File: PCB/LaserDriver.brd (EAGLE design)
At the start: 160 x 100 mm, 23 parts, among them IC1 OPA27U, IC2 7805T, Q1 IRF510

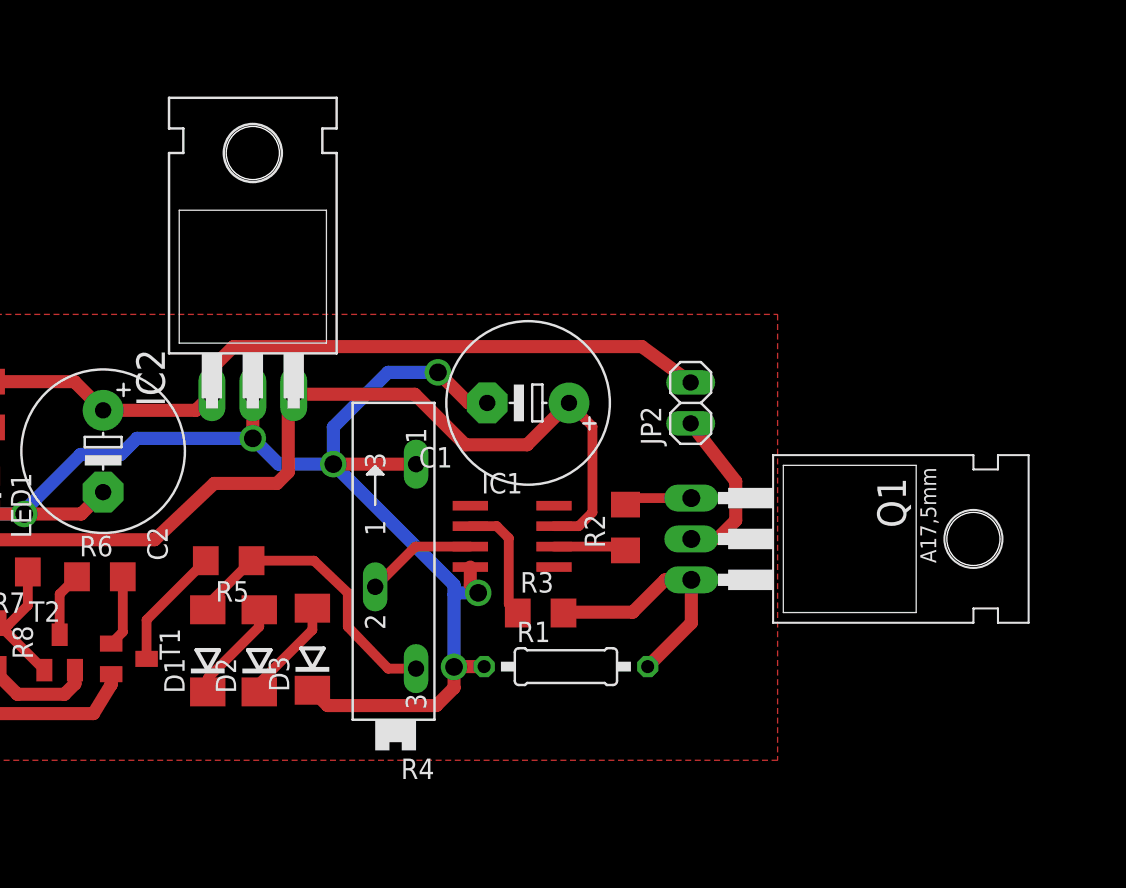
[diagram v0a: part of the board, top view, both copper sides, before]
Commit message: Fixed component placement issues and modified directory tree.
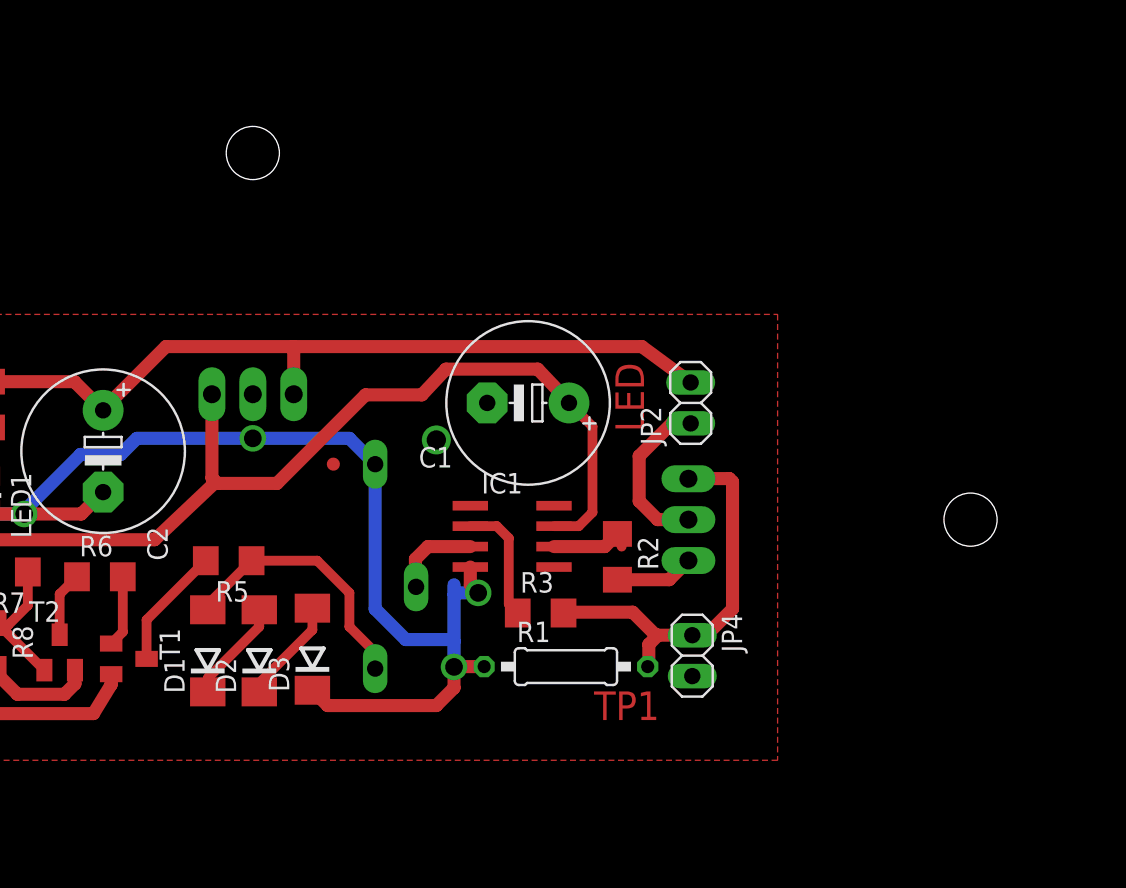
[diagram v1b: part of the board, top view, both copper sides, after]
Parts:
- added JP4: (no value), pinhead:1X02
- moved R2 1.89 mm to (58.4, 32.9), turned to 270 degrees
- moved Q1 1.21 mm to (69.1, 35.2), flipped to the bottom, turned to 90 degrees
- flipped IC2 to the bottom
- flipped R4 to the bottom
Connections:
- net GND: now also JP4.2
- net N$1: now also JP4.1
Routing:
- net GND: track 119.2 -> 104.0 mm, vias 8 -> 6
- net N$1: track 15.3 -> 24.8 mm
- net VCC: track 85.7 -> 87.9 mm
- net N$15: track 52.6 -> 54.7 mm
- net N$6: track 18.4 -> 16.5 mm
- net N$5: track 6.95 -> 5.42 mm
- net N$2: track 4.26 -> 4.90 mm
- net N$4: track 4.54 -> 5.10 mm
- added copper zone on layer 1, net GND
- removed copper zone on layer 1, net N$17
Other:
- board text added: "LED"
- board text added: "TP1"

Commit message: Added possibility set print sweep time. Fixed laser driver layout.
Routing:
- net GND: vias 6 -> 7
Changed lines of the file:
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@@
 <wire x1="35.7" y1="40.3" x2="41.695" y2="40.3" width="0.8128" layer="16"/>
 <wire x1="41.695" y1="40.3" x2="43.3" y2="38.695" width="0.8128" layer="16"/>
+<via x="47.1" y="40.2" extent="1-16" drill="1.2" shape="octagon"/>
+<wire x1="50.26" y1="42.5" x2="47.1" y2="40.2" width="0" layer="19" extent="1-1"/>
 </signal>
 <signal name="N$1">
@@
 <wire x1="19.4" y1="40.978" x2="19.4" y2="37.95" width="0.6096" layer="1"/>
 </signal>
-<signal name="N$17">
-<via x="47.1" y="40.2" extent="1-16" drill="1.2" shape="octagon"/>
-</signal>
 </signals>
